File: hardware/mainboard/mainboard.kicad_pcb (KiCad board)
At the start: 4 copper layers, 100 x 60 mm, 52 parts, among them J1 USB-C, J2 4.3" RGB panel, J3 GT911 touch, J4 SparkFun 2D Barcode Scanner, J5 UART scanner (GM65), J6 LD2410C radar, Q1 AO3400A, SW1 RESET, SW2 BOOT, U1 USBLC6-2SC6, U2 SY8089AAAC, U3 ESP32-S3-WROOM-1-N16R8, U4 74AHCT1G125, U5 TPS61169

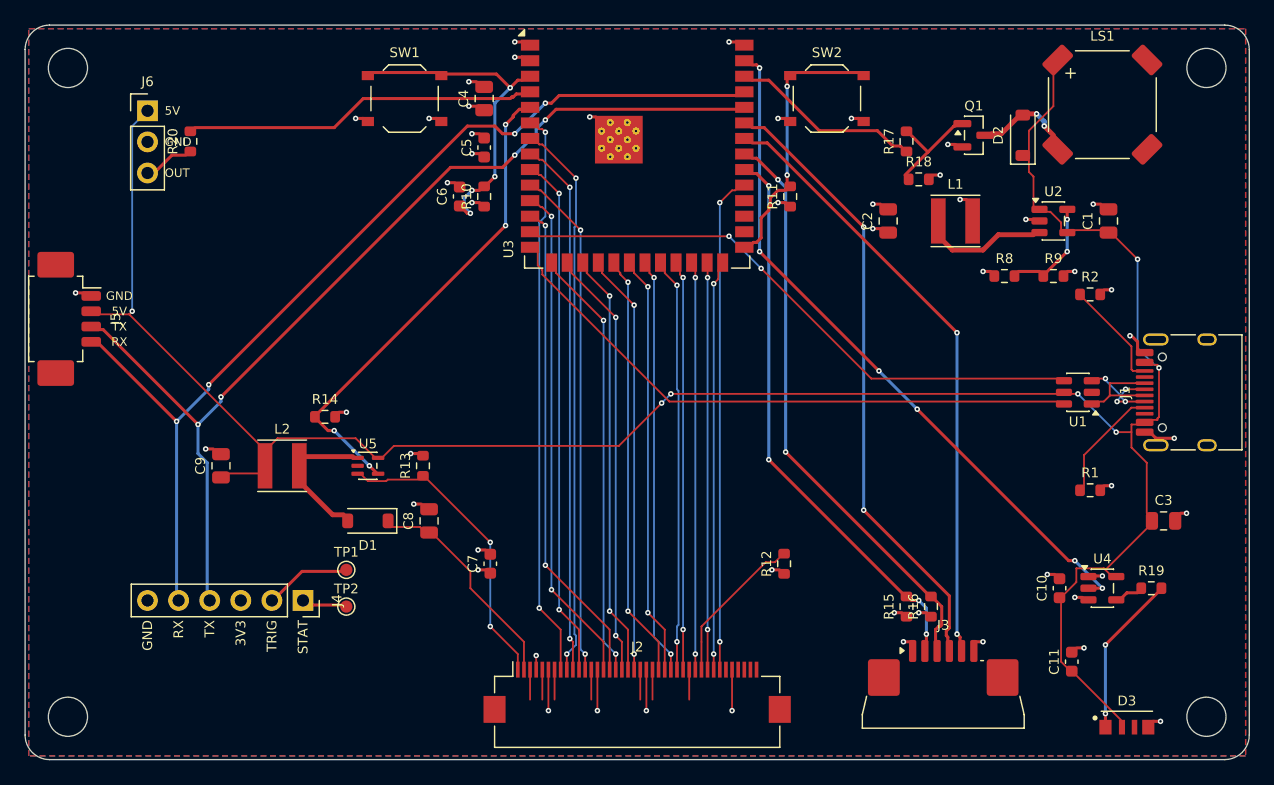
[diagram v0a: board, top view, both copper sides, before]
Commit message: Drop the presence radar
A scan already wakes the screen, so the LD2410C radar only saved a glance at
the dim clock. Gone from:

- firmware: pantry-feedback.yaml no longer has the presence sensor; the
  carrier package loses the radar UART and ld2410
- scanner carrier: the 5-pin radar header, its three resistors and the
  Sunton P2 connector it needed (two cables to the Sunton now, not three)
- mainboard: the radar header and its resistor; IO4 is free
- enclosure: the radar rails; the chin shrinks to 15 mm, so the case is
  now 111 x 139 x 51 mm

Both boards rebuilt clean (ERC 0, DRC 0 / 0 unconnected / 0 footprint
errors). On the mainboard the ribbon connector is now the only part whose
fine-pitch ground pins rely on the pour; U5's narrow ground pin gets a via
again. All four firmware configs validate.
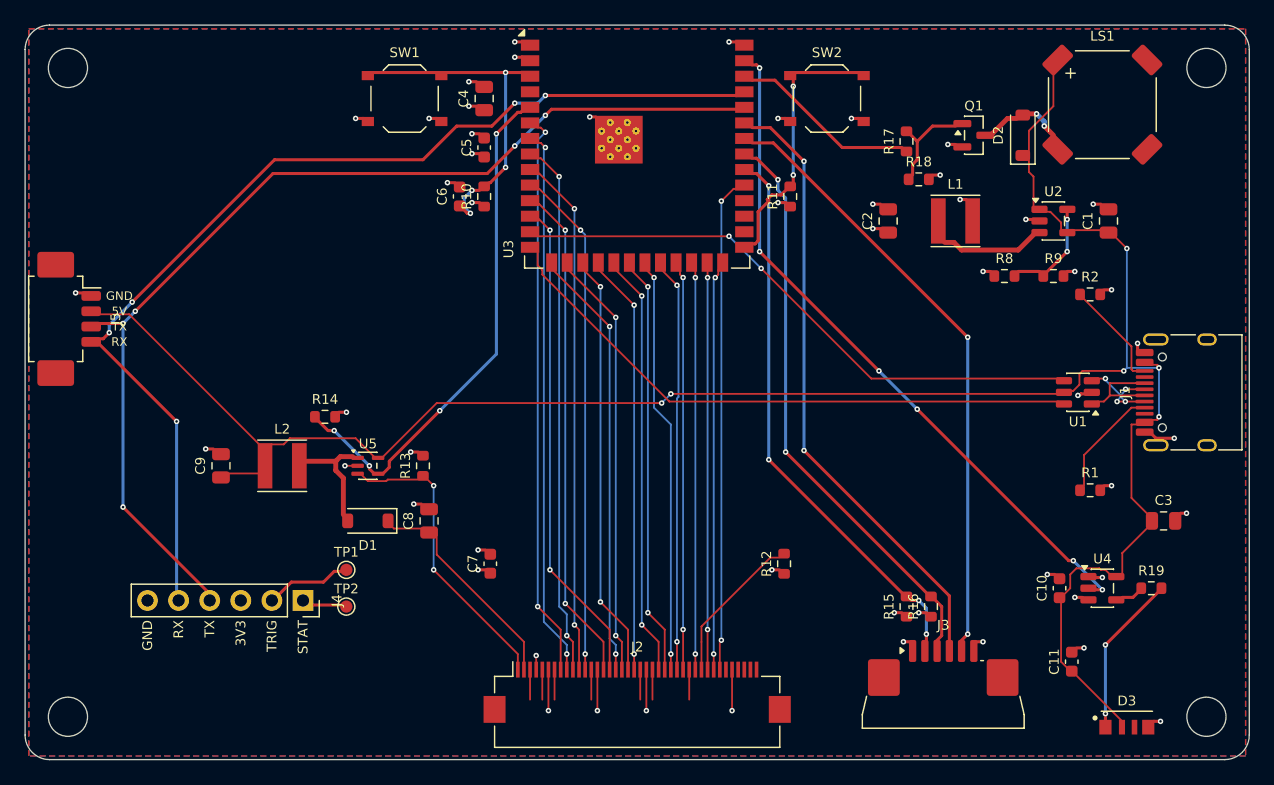
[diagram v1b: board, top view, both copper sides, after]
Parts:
- removed J6: LD2410C radar, Connector_PinHeader_2.54mm:PinHeader_1x03_P2.54mm_Vertical
- removed R20: 1k, Resistor_SMD:R_0603_1608Metric
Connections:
- U3 pad 4: /PRESENCE -> unconnected-(U3-IO4-Pad4)
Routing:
- net /PRESENCE: track 27.9 -> 0.00 mm
- net /+5V: track 171.7 -> 156.4 mm, vias 7 -> 6
- net /SCAN_TX: track 80.3 -> 84.0 mm, vias 4 -> 5
- net /SCAN_RX: track 80.2 -> 83.3 mm, vias 4 -> 5
- net /RADAR_OUT: track 2.89 -> 0.00 mm
- net /BL_PWM: track 38.3 -> 40.9 mm
- net /TP_INT: track 48.5 -> 49.3 mm
- net /BL_SW: track 7.93 -> 8.66 mm
- net /R4: track 44.5 -> 43.9 mm
- net /GND: track 53.3 -> 53.6 mm, vias 37 -> 39
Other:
- board text removed: "OUT"
